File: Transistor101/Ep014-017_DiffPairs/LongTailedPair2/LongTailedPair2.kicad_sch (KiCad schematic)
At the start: 17 parts, among them J1 AWG channel 1, J2 AWG channel 2, J3 Output to oscilloscope, Q1 DMMT5551, Q2 DMMT5551, T1 SEE NOTES

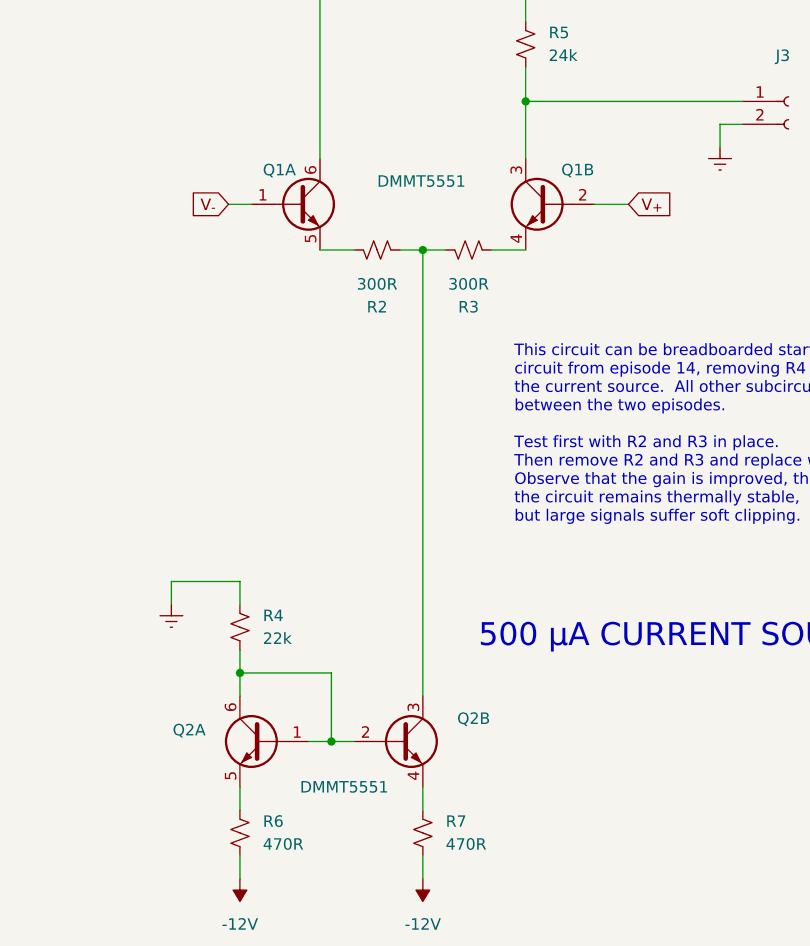
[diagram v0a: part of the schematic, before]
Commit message: Correct pinout of DMMT5401
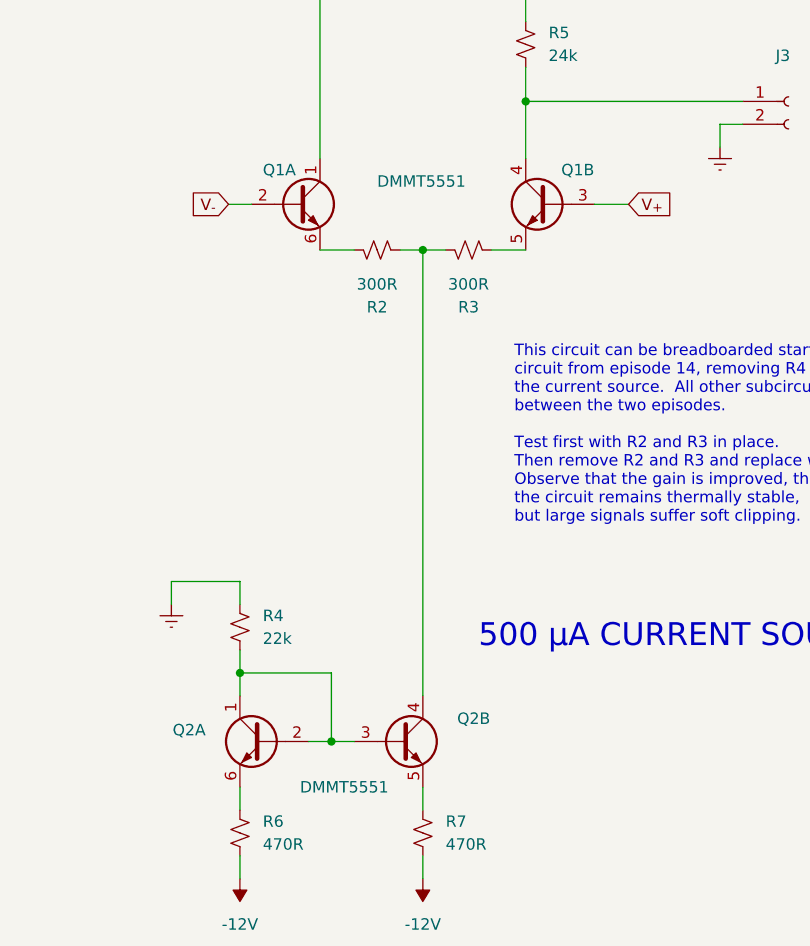
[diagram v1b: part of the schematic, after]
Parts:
- Q1, Q2: footprint (none) -> Package_TO_SOT_SMD:SOT-363_SC-70-6; symbol Kevin-Transistors:Q_Dual_NPN_NPN_B1B2C2E2E1C1 -> Kevin-Transistors:DMMT5551
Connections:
- net +12V: now also Q1.1 (C1); no longer Q1.6 (C1)
- net V_{+}: now also Q1.3 (B2); no longer Q1.2 (B2)
- net V_{-}: now also Q1.2 (B1); no longer Q1.1 (B1)
- net at R6.1: now also Q2.6 (E1); no longer Q2.5 (E1)
- net at R2.1: now also Q1.6 (E1); no longer Q1.5 (E1)
- net at R2.2, R3.1: now also Q2.4 (C2); no longer Q2.3 (C2)
- net at Q2.1 (C1), R4.2: now also Q2.2 (B1), Q2.3 (B2); no longer Q2.2 (B2), Q2.6 (C1)
- net at J3.1 (Pin_1), R5.2: now also Q1.4 (C2); no longer Q1.3 (C2)
- net at R3.2: now also Q1.5 (E2); no longer Q1.4 (E2)
- net at R7.1: now also Q2.5 (E2); no longer Q2.4 (E2)
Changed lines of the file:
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@@
   (title_block
     (title "Long-tailed pair: the basic circuit")
-    (date "2025-02-08")
+    (date "2026-05-13")
     (rev "B")
     (company "Kludges from Kevin's Cave")
@@
     )
   )
-  (symbol (lib_id "Kevin-Transistors:Q_Dual_NPN_NPN_B1B2C2E2E1C1") (at 144.78 132.08 0) (mirror y) (unit 1)
+  (symbol (lib_id "Kevin-Transistors:DMMT5551") (at 144.78 132.08 0) (mirror y) (unit 1)
     (in_bom yes) (on_board yes) (dnp no)
     (property "Reference" "Q2" (at 138.43 130.81 0)
@@
       (effects (font (size 1.27 1.27)) (justify left))
     )
-    (property "Footprint" "" (at 139.7 129.54 0)
-      (effects (font (size 1.27 1.27)) hide)
-    )
-    (property "Datasheet" "~" (at 144.78 132.08 0)
+    (property "Footprint" "Package_TO_SOT_SMD:SOT-363_SC-70-6" (at 139.7 129.54 0)
+      (effects (font (size 1.27 1.27)) hide)
+    )
+    (property "Datasheet" "https://www.diodes.com/assets/Datasheets/ds30436.pdf" (at 144.78 132.08 0)
       (effects (font (size 1.27 1.27)) hide)
     )
@@
     )
   )
-  (symbol (lib_id "Kevin-Transistors:Q_Dual_NPN_NPN_B1B2C2E2E1C1") (at 176.53 72.39 0) (mirror y) (unit 2)
+  (symbol (lib_id "Kevin-Transistors:DMMT5551") (at 176.53 72.39 0) (mirror y) (unit 2)
     (in_bom yes) (on_board yes) (dnp no)
     (property "Reference" "Q1" (at 181.61 68.58 0)
@@
       (effects (font (size 1.27 1.27)) (justify left) hide)
     )
-    (property "Footprint" "" (at 171.45 69.85 0)
-      (effects (font (size 1.27 1.27)) hide)
-    )
-    (property "Datasheet" "~" (at 176.53 72.39 0)
+    (property "Footprint" "Package_TO_SOT_SMD:SOT-363_SC-70-6" (at 171.45 69.85 0)
+      (effects (font (size 1.27 1.27)) hide)
+    )
+    (property "Datasheet" "https://www.diodes.com/assets/Datasheets/ds30436.pdf" (at 176.53 72.39 0)
       (effects (font (size 1.27 1.27)) hide)
     )
@@
     )
   )
-  (symbol (lib_id "Kevin-Transistors:Q_Dual_NPN_NPN_B1B2C2E2E1C1") (at 160.02 132.08 0) (unit 2)
+  (symbol (lib_id "Kevin-Transistors:DMMT5551") (at 160.02 132.08 0) (unit 2)
     (in_bom yes) (on_board yes) (dnp no)
     (property "Reference" "Q2" (at 166.37 129.54 0)
@@
       (effects (font (size 1.27 1.27)) (justify left) hide)
     )
-    (property "Footprint" "" (at 165.1 129.54 0)
-      (effects (font (size 1.27 1.27)) hide)
-    )
-    (property "Datasheet" "~" (at 160.02 132.08 0)
+    (property "Footprint" "Package_TO_SOT_SMD:SOT-363_SC-70-6" (at 165.1 129.54 0)
+      (effects (font (size 1.27 1.27)) hide)
+    )
+    (property "Datasheet" "https://www.diodes.com/assets/Datasheets/ds30436.pdf" (at 160.02 132.08 0)
       (effects (font (size 1.27 1.27)) hide)
     )
@@
     )
   )
-  (symbol (lib_id "Kevin-Transistors:Q_Dual_NPN_NPN_B1B2C2E2E1C1") (at 148.59 72.39 0) (unit 1)
+  (symbol (lib_id "Kevin-Transistors:DMMT5551") (at 148.59 72.39 0) (unit 1)
     (in_bom yes) (on_board yes) (dnp no)
     (property "Reference" "Q1" (at 144.78 68.58 0)
@@
       (effects (font (size 1.27 1.27)) (justify left))
     )
-    (property "Footprint" "" (at 153.67 69.85 0)
-      (effects (font (size 1.27 1.27)) hide)
-    )
-    (property "Datasheet" "~" (at 148.59 72.39 0)
-      (effects (font (size 1.27 1.27)) hide)
-    )
+    (property "Footprint" "Package_TO_SOT_SMD:SOT-363_SC-70-6" (at 153.67 69.85 0)
+      (effects (font (size 1.27 1.27)) hide)
+    )
+    (property "Datasheet" "https://www.diodes.com/assets/Datasheets/ds30436.pdf" (at 148.59 72.39 0)
+      (effects (font (size 1.27 1.27)) hide)
+    )
